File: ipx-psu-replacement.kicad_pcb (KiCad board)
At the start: 2 copper layers, 226 x 81 mm, 31 parts, among them J1 L, J10 -12V, J11 GND, J12 Fan, J13 SENS, J14 GND, J15 GND, J2 AC IN, J3 GND, J4 Floppy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

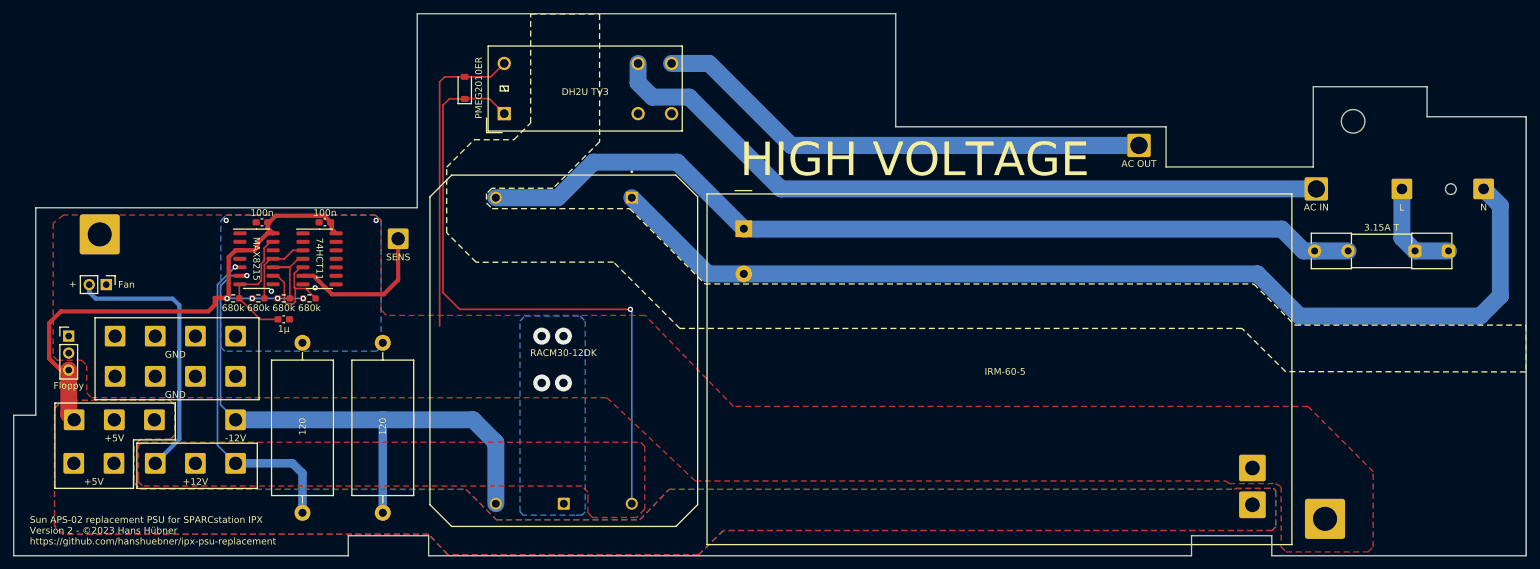
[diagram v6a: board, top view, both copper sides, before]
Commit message: correct mounting hole locations
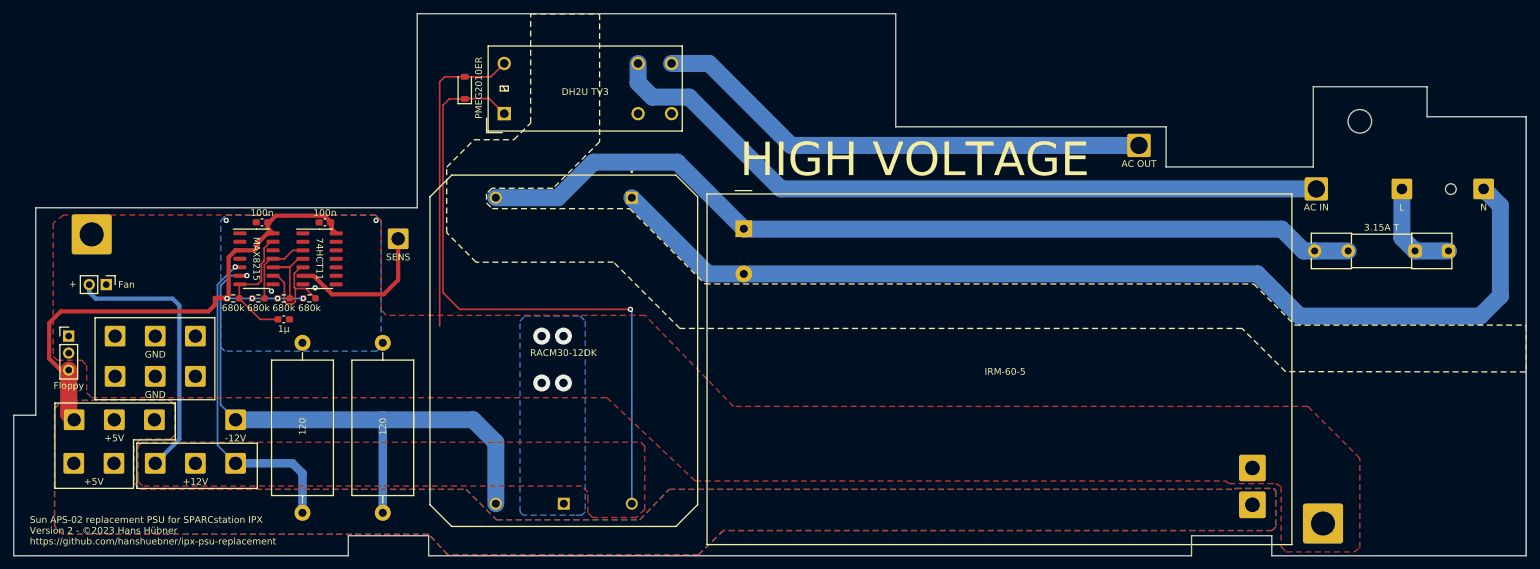
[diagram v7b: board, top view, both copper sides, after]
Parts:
- J11, J3: footprint Connector_Wire:SolderWire-1.5sqmm_1x04_P6mm_D1.7mm_OD3mm -> Connector_Wire:SolderWire-1.5sqmm_1x03_P6mm_D1.7mm_OD3mm
- moved J14 1.20 mm to (51.0, 91.8)
- moved J15 0.76 mm to (235.0, 135.0)
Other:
- outline, holes or cut-outs redrawn
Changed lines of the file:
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@@
   )
   (footprint "Connector_Wire:SolderWire-2sqmm_1x01_D2mm_OD3.9mm" (layer "F.Cu")
-    (at 52.2 91.8 180)
+    (at 51 91.8 180)
     (descr "Soldered wire connection, for a single 2 mm² wire, reinforced insulation, conductor diameter 2mm, outer diameter 3.9mm, size source Multi-Contact FLEXI-xV 2.0 (https://ec.staubli.com/AcroFiles/Catalogues/TM_Cab-Main-11014119_(en)_hi.pdf), bend radius 3 times outer diameter, generated with kicad-footprint-generator")
     (tags "connector wire 2sqmm")
@@
     )
   )
-  (footprint "Connector_Wire:SolderWire-1.5sqmm_1x04_P6mm_D1.7mm_OD3mm" (layer "F.Cu")
+  (footprint "Connector_Wire:SolderWire-1.5sqmm_1x03_P6mm_D1.7mm_OD3mm" (layer "F.Cu")
     (at 54.5 107)
-    (descr "Soldered wire connection, for 4 times 1.5 mm² wires, basic insulation, conductor diameter 1.7mm, outer diameter 3mm, size source Multi-Contact FLEXI-E 1.5 (https://ec.staubli.com/AcroFiles/Catalogues/TM_Cab-Main-11014119_(en)_hi.pdf), bend radius 3 times outer diameter, generated with kicad-footprint-generator")
+    (descr "Soldered wire connection, for 3 times 1.5 mm² wires, basic insulation, conductor diameter 1.7mm, outer diameter 3mm, size source Multi-Contact FLEXI-E 1.5 (https://ec.staubli.com/AcroFiles/Catalogues/TM_Cab-Main-11014119_(en)_hi.pdf), bend radius 3 times outer diameter, generated with kicad-footprint-generator")
     (tags "connector wire 1.5sqmm")
     (property "Sheetfile" "ipx-psu-replacement.kicad_sch")
     (property "Sheetname" "")
-    (property "ki_description" "Generic connector, single row, 01x04, script generated")
+    (property "ki_description" "Generic connector, single row, 01x03, script generated")
     (property "ki_keywords" "connector")
-    (attr exclude_from_pos_files)
-    (fp_text reference "J11" (at 9 -2.75) (layer "F.SilkS") hide
-        (effects (font (size 1 1) (thickness 0.15)))
-    )
-    (fp_text value "GND" (at 9 2.75) (layer "F.SilkS")
-        (effects (font (size 1 1) (thickness 0.15)))
-    )
-    (fp_text user "${REFERENCE}" (at 9 0 90) (layer "F.Fab") hide
-        (effects (font (size 1 1) (thickness 0.15)))
+    (attr exclude_from_pos_files exclude_from_bom)
+    (fp_text reference "J11" (at 6 -2.75) (layer "F.SilkS") hide
+        (effects (font (size 1 1) (thickness 0.15)))
+    )
+    (fp_text value "GND" (at 6 2.75) (layer "F.SilkS")
+        (effects (font (size 1 1) (thickness 0.15)))
+    )
+    (fp_text user "${REFERENCE}" (at 6 0) (layer "F.Fab") hide
+        (effects (font (size 0.75 0.75) (thickness 0.11)))
     )
     (fp_line (start -2.25 -2.05) (end -2.25 2.05)
@@
     (fp_line (start 14.25 2.05) (end 14.25 -2.05)
       (stroke (width 0.05) (type solid)) (layer "F.CrtYd"))
-    (fp_line (start 15.75 -2.05) (end 15.75 2.05)
-      (stroke (width 0.05) (type solid)) (layer "F.CrtYd"))
-    (fp_line (start 15.75 2.05) (end 20.25 2.05)
-      (stroke (width 0.05) (type solid)) (layer "F.CrtYd"))
-    (fp_line (start 20.25 -2.05) (end 15.75 -2.05)
-      (stroke (width 0.05) (type solid)) (layer "F.CrtYd"))
-    (fp_line (start 20.25 2.05) (end 20.25 -2.05)
-      (stroke (width 0.05) (type solid)) (layer "F.CrtYd"))
     (fp_circle (center 0 0) (end 1.5 0)
       (stroke (width 0.1) (type solid)) (fill none) (layer "F.Fab"))
@@
     (fp_circle (center 12 0) (end 13.5 0)
       (stroke (width 0.1) (type solid)) (fill none) (layer "F.Fab"))
-    (fp_circle (center 18 0) (end 19.5 0)
-      (stroke (width 0.1) (type solid)) (fill none) (layer "F.Fab"))
-    (pad "1" thru_hole roundrect (at 0 0) (size 3.1 3.1) (drill 2) (layers "*.Cu" "*.Mask") (roundrect_rratio 0.08)
+    (pad "1" thru_hole roundrect (at 0 0) (size 3.1 3.1) (drill 2) (layers "*.Cu" "*.Mask") (roundrect_rratio 0.080645)
       (net 3 "GND") (pinfunction "Pin_1") (pintype "passive"))
     (pad "2" thru_hole roundrect (at 6 0) (size 3.1 3.1) (drill 2) (layers "*.Cu" "*.Mask") (roundrect_rratio 0.08)
@@
     (pad "3" thru_hole roundrect (at 12 0) (size 3.1 3.1) (drill 2) (layers "*.Cu" "*.Mask") (roundrect_rratio 0.08)
       (net 3 "GND") (pinfunction "Pin_3") (pintype "passive"))
-    (pad "4" thru_hole roundrect (at 18 0) (size 3.1 3.1) (drill 2) (layers "*.Cu" "*.Mask") (roundrect_rratio 0.08)
-      (net 3 "GND") (pinfunction "Pin_4") (pintype "passive"))
-    (model "${KICAD6_3DMODEL_DIR}/Connector_Wire.3dshapes/SolderWire-1.5sqmm_1x04_P6mm_D1.7mm_OD3mm.wrl"
+    (model "${KICAD6_3DMODEL_DIR}/Connector_Wire.3dshapes/SolderWire-1.5sqmm_1x03_P6mm_D1.7mm_OD3mm.wrl"
       (offset (xyz 0 0 0))
       (scale (xyz 1 1 1))
@@
     )
   )
-  (footprint "Connector_Wire:SolderWire-1.5sqmm_1x04_P6mm_D1.7mm_OD3mm" (layer "F.Cu")
+  (footprint "Connector_Wire:SolderWire-1.5sqmm_1x03_P6mm_D1.7mm_OD3mm" (layer "F.Cu")
     (at 54.5 113)
-    (descr "Soldered wire connection, for 4 times 1.5 mm² wires, basic insulation, conductor diameter 1.7mm, outer diameter 3mm, size source Multi-Contact FLEXI-E 1.5 (https://ec.staubli.com/AcroFiles/Catalogues/TM_Cab-Main-11014119_(en)_hi.pdf), bend radius 3 times outer diameter, generated with kicad-footprint-generator")
+    (descr "Soldered wire connection, for 3 times 1.5 mm² wires, basic insulation, conductor diameter 1.7mm, outer diameter 3mm, size source Multi-Contact FLEXI-E 1.5 (https://ec.staubli.com/AcroFiles/Catalogues/TM_Cab-Main-11014119_(en)_hi.pdf), bend radius 3 times outer diameter, generated with kicad-footprint-generator")
     (tags "connector wire 1.5sqmm")
     (property "Sheetfile" "ipx-psu-replacement.kicad_sch")
     (property "Sheetname" "")
-    (property "ki_description" "Generic connector, single row, 01x04, script generated")
+    (property "ki_description" "Generic connector, single row, 01x03, script generated")
     (property "ki_keywords" "connector")
-    (attr exclude_from_pos_files)
-    (fp_text reference "J3" (at 9 -2.75) (layer "F.SilkS") hide
-        (effects (font (size 1 1) (thickness 0.15)))
-    )
-    (fp_text value "GND" (at 9 2.75) (layer "F.SilkS")
-        (effects (font (size 1 1) (thickness 0.15)))
-    )
-    (fp_text user "${REFERENCE}" (at 9 0 90) (layer "F.Fab") hide
-        (effects (font (size 1 1) (thickness 0.15)))
+    (attr exclude_from_pos_files exclude_from_bom)
+    (fp_text reference "J3" (at 6 -2.75) (layer "F.SilkS") hide
+        (effects (font (size 1 1) (thickness 0.15)))
+    )
+    (fp_text value "GND" (at 6 2.75) (layer "F.SilkS")
+        (effects (font (size 1 1) (thickness 0.15)))
+    )
+    (fp_text user "${REFERENCE}" (at 6 0) (layer "F.Fab") hide
+        (effects (font (size 0.75 0.75) (thickness 0.11)))
     )
     (fp_line (start -2.25 -2.05) (end -2.25 2.05)
@@
     (fp_line (start 14.25 2.05) (end 14.25 -2.05)
       (stroke (width 0.05) (type solid)) (layer "F.CrtYd"))
-    (fp_line (start 15.75 -2.05) (end 15.75 2.05)
-      (stroke (width 0.05) (type solid)) (layer "F.CrtYd"))
-    (fp_line (start 15.75 2.05) (end 20.25 2.05)
-      (stroke (width 0.05) (type solid)) (layer "F.CrtYd"))
-    (fp_line (start 20.25 -2.05) (end 15.75 -2.05)
-      (stroke (width 0.05) (type solid)) (layer "F.CrtYd"))
-    (fp_line (start 20.25 2.05) (end 20.25 -2.05)
-      (stroke (width 0.05) (type solid)) (layer "F.CrtYd"))
     (fp_circle (center 0 0) (end 1.5 0)
       (stroke (width 0.1) (type solid)) (fill none) (layer "F.Fab"))
@@
     (fp_circle (center 12 0) (end 13.5 0)
       (stroke (width 0.1) (type solid)) (fill none) (layer "F.Fab"))
-    (fp_circle (center 18 0) (end 19.5 0)
-      (stroke (width 0.1) (type solid)) (fill none) (layer "F.Fab"))
-    (pad "1" thru_hole roundrect (at 0 0) (size 3.1 3.1) (drill 2) (layers "*.Cu" "*.Mask") (roundrect_rratio 0.08)
+    (pad "1" thru_hole roundrect (at 0 0) (size 3.1 3.1) (drill 2) (layers "*.Cu" "*.Mask") (roundrect_rratio 0.080645)
       (net 3 "GND") (pinfunction "Pin_1") (pintype "passive"))
     (pad "2" thru_hole roundrect (at 6 0) (size 3.1 3.1) (drill 2) (layers "*.Cu" "*.Mask") (roundrect_rratio 0.08)
@@
     (pad "3" thru_hole roundrect (at 12 0) (size 3.1 3.1) (drill 2) (layers "*.Cu" "*.Mask") (roundrect_rratio 0.08)
       (net 3 "GND") (pinfunction "Pin_3") (pintype "passive"))
-    (pad "4" thru_hole roundrect (at 18 0) (size 3.1 3.1) (drill 2) (layers "*.Cu" "*.Mask") (roundrect_rratio 0.08)
-      (net 3 "GND") (pinfunction "Pin_4") (pintype "passive"))
-    (model "${KICAD6_3DMODEL_DIR}/Connector_Wire.3dshapes/SolderWire-1.5sqmm_1x04_P6mm_D1.7mm_OD3mm.wrl"
+    (model "${KICAD6_3DMODEL_DIR}/Connector_Wire.3dshapes/SolderWire-1.5sqmm_1x03_P6mm_D1.7mm_OD3mm.wrl"
       (offset (xyz 0 0 0))
       (scale (xyz 1 1 1))
@@
   )
   (footprint "Connector_Wire:SolderWire-2sqmm_1x01_D2mm_OD3.9mm" (layer "F.Cu")
-    (at 235.3 134.3)
+    (at 235 135)
     (descr "Soldered wire connection, for a single 2 mm² wire, reinforced insulation, conductor diameter 2mm, outer diameter 3.9mm, size source Multi-Contact FLEXI-xV 2.0 (https://ec.staubli.com/AcroFiles/Catalogues/TM_Cab-Main-11014119_(en)_hi.pdf), bend radius 3 times outer diameter, generated with kicad-footprint-generator")
     (tags "connector wire 2sqmm")
@@
     (pts
       (xy 51.5 104.25)
-      (xy 76 104.25)
-      (xy 76 116.5)
+      (xy 69.4 104.25)
+      (xy 69.4 116.5)
       (xy 51.5 116.5)
     )
@@
   (gr_line (start 233.55 69.72) (end 250.55 69.72)
     (stroke (width 0.1) (type default)) (layer "Edge.Cuts"))
-  (gr_circle (center 239.5 74.9) (end 241.26 74.9)
+  (gr_circle (center 240.5 74.9) (end 242.26 74.9)
     (stroke (width 0.1) (type default)) (fill none) (layer "Edge.Cuts"))
   (gr_line (start 42.65 87.82) (end 42.65 118.82)
@@
         (xy 228.744711 138.5)
         (xy 229.5 139.25)
-        (xy 241.75 139.25)
-        (xy 242.5 138.5)
-        (xy 242.5 127.25)
+        (xy 239.666668 139.25)
+        (xy 240.5 138.625001)
+        (xy 240.5 125.25)
         (xy 232.75 117.5)
         (xy 146.9 117.5)
